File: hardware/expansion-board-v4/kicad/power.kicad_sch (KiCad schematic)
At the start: 39 parts, among them J9 MX1.25WT-2P BAT, U1 ME6211C33M5, U18 CH224K, U19 SY6970, U2 TPS7A2033PDBVR, U20 SY7069, U3 TPS7A2033PDBVR

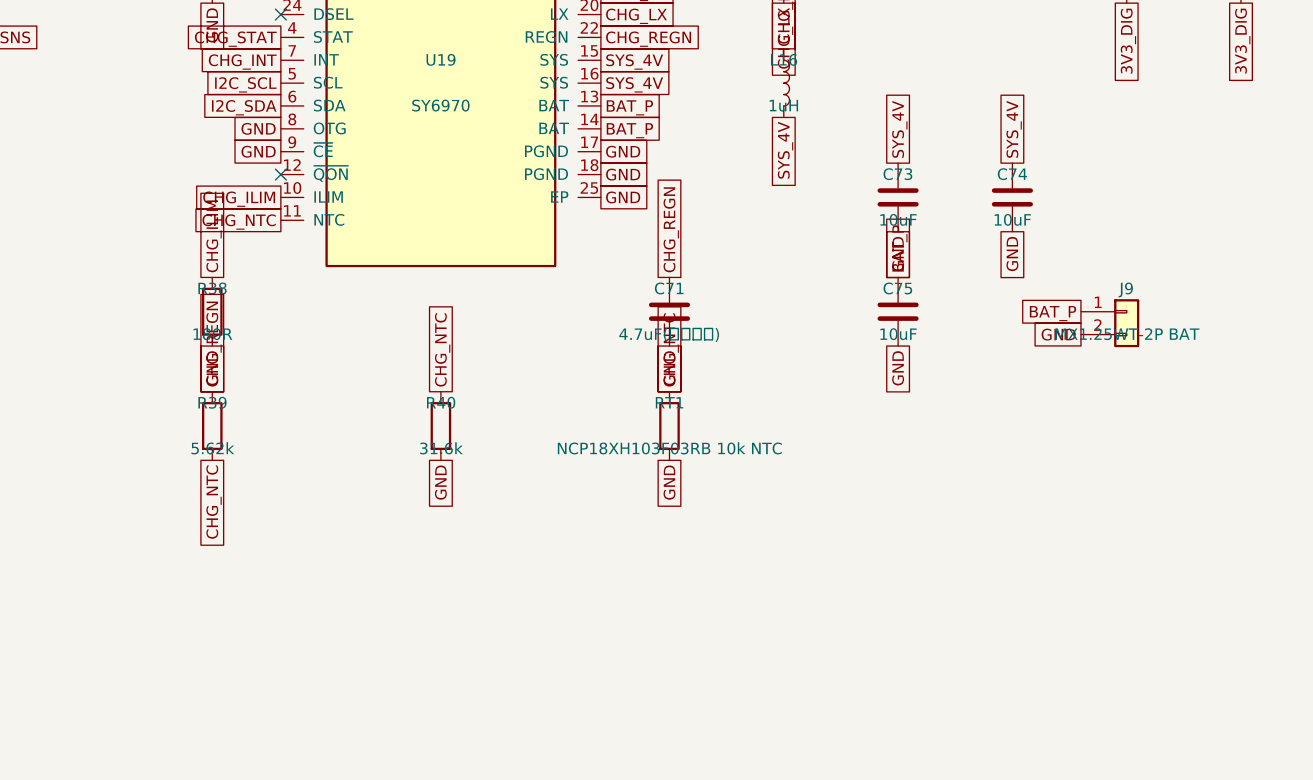
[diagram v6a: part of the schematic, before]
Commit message: v4.7: SW3 主电源键接 /QON + TCXO 输出隔直 + 覆铜填充参数固化
**SW3 主电源键**。电池在位时 SYS 恒供电，整板此前没有任何机械总电门：
微雪 Key3 只关得掉载板自己，而整机 5V 是扩展板升压产的；J1 的 40 脚里
没有一根电源控制线。唯一出路是 SY6970 的 BATFET——所以引 U19.12(/QON)
到板边的 TS24CA 侧按键（按住 1.25~2.25s 开机，BUS 拔掉时按 12~18s 硬复位），
不依赖固件。摆在 USB 口同侧贴板边 (97.882, 39.103)，R7/R8 那组往板内让 4mm 腾位。

封装按规格书 1:1：电气端子 1.2×0.6 中心距 3.4、固定脚 1.3×1.05 外缘跨度 5.3、
两个 φ0.55 定位孔在 X+0.70。两个坑记在封装 descr 里：①定位孔的 layers 必须写
「*.Cu」而不是「F&B.Cu」，否则 6 层板的内层覆铜照样压上来（每孔 5 条
hole_clearance、实际间距 0）；②孔心不能按「上下排焊盘空档的中心」推，那样
错 0.75mm、柱子插不进去。

**TCXO 输出隔直**。Epson brief sheet 的输出负载条件栏写死 DC cut = 0.01µF，
原设计 Y4.3 直连 BK4819 的 XI。补 C99(0402 100pF C0G) 串联 + R61(0402 10k)
负载，VHF_TCXO 拆成 VHF_TCXO_OUT / VHF_TCXO 两网。这里只能用 0402：两焊盘
净空 2.28mm，0603 含焊盘约 2.8mm 放不下，而 Y4 四周被 C76/C98/U21 夹死挪不开。
Y4 符号 pin1 由 EN 改 NC（选型库 fcfYN=N，无压控，悬空正确）。

**覆铜填充参数固化**（本次真正的回归修复）。ZONES.json 此前不含 fill 参数，
重放时 clearance 从板上的 0.15 退回 KiCad 默认 0.5，结果是 2 条网络断开、
4 个悬空端、4 个焊盘未连通——而 DRC 报 0 违例。「DRC 全绿」和「板子是错的」
可以同时成立，因为 zone 的 local clearance 不是 DRC 可见参数。现在导出/回填
clearance、min_thickness、pad_connection、thermal_gap/spoke、island_removal，
并加门禁：任何非 rule-area 的 zone 没拿到固化参数就炸。

装配助手加 v4.7-pwr / v4.7-nopwr，v4.6-* 转归档（元件数据不动，只在副标题
注明「无 SW3 电源键」）。SW3 属于电源区，不带电源版不贴它：207/82 → 180/67。

英文同步器补阶段 G（Airband）并加未登记阶段即炸的护栏：此前中文表加了 G，
而这里只认 A–F，stage 变量保持上一轮的 F 不变，19 个 airband 件被整段并进
「Stage F: External Interface」（1 件变 20 件），两边都不报错、产物看着完整。

Gerber/源包重出为 V4.7-20260913（制造内容与先前那版逐字节相同，仅时间戳行
不同；源包重出是为了让包内 PCB 与工作树一致）。

hardware 契约 80 条：76 通过、4 条 expansion-board-v3 的 RP_1V1 既存豁免不在
本次范围。interface.kicad_sch 工作树里有一份纯 uuid 变更、来源不明，未纳入。
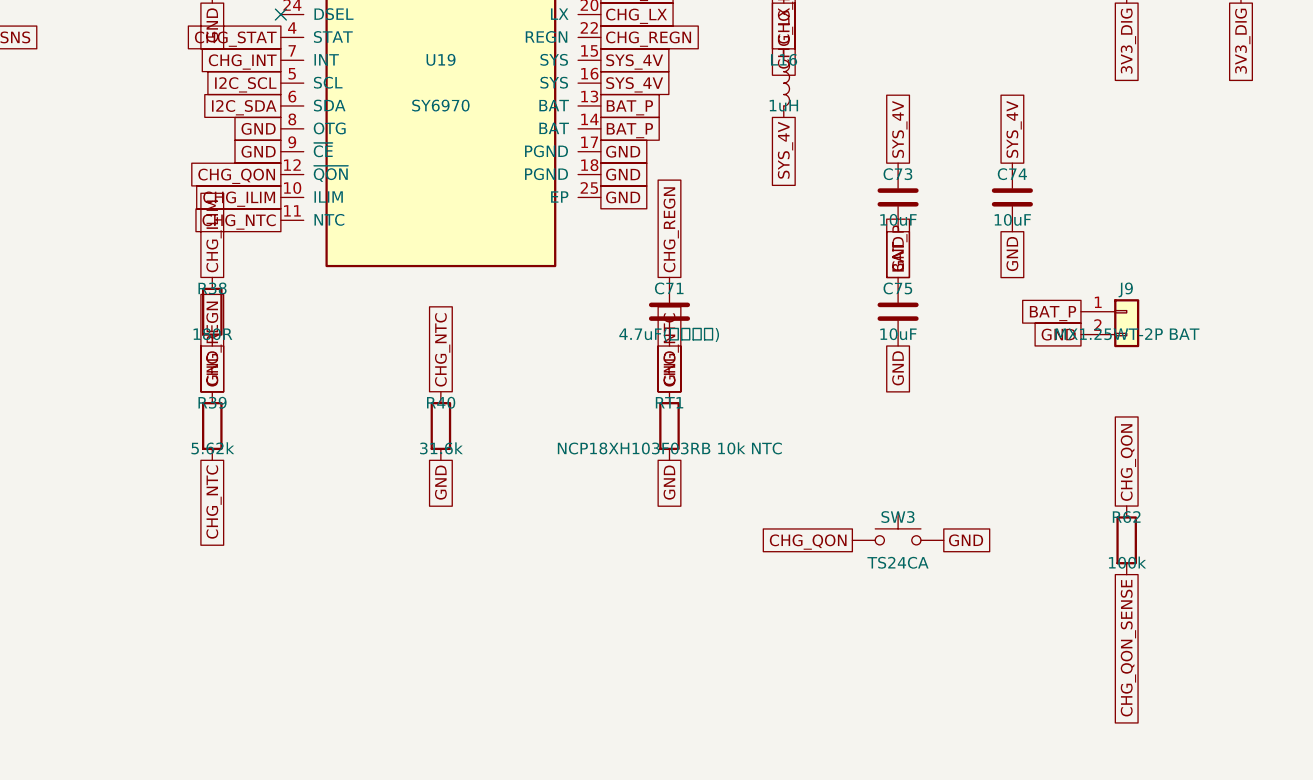
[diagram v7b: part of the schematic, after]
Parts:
- added R62: 100k, Resistor_SMD:R_0603_1608Metric, symbol Device:R
- added SW3: TS24CA, expansion-board-v4:SW_TS24CA_2x4_SideAct, symbol Switch:SW_Push
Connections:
- net GND: now also SW3.2
- net CHG_QON: now reaches U19.12 (~{QON})
- net CHG_QON: now also R62.1, SW3.1
- new net CHG_QON_SENSE: R62.2
- no-connect marks 10 -> 9
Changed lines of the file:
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@@
 		(effects (font (size 1.27 1.27)) (justify right))
 	)
-	(no_connect
-		(at 134.62 175.26)
+	(global_label "CHG_QON"
+		(shape passive)
+		(at 134.62 175.26 180)
+		(effects (font (size 1.27 1.27)) (justify right))
 	)
 	(global_label "CHG_ILIM"
@@
 		(effects (font (size 1.27 1.27)) (justify right))
 	)
+	(symbol
+		(lib_id "Switch:SW_Push")
+		(at 203.2 215.9 0)
+		(unit 1)
+		(exclude_from_sim no)
+		(in_bom yes)
+		(on_board yes)
+		(dnp no)
+		(property "Reference" "SW3"
+			(at 203.2 213.36 0)
+			(effects (font (size 1.27 1.27)))
+		)
+		(property "Value" "TS24CA"
+			(at 203.2 218.44 0)
+			(effects (font (size 1.27 1.27)))
+		)
+		(property "Footprint" "expansion-board-v4:SW_TS24CA_2x4_SideAct"
+			(at 203.2 220.98 0)
+			(effects (font (size 1.27 1.27))
+				(hide yes))
+		)
+		(property "Datasheet" "~"
+			(at 203.2 223.52 0)
+			(effects (font (size 1.27 1.27))
+				(hide yes))
+		)
+		(pin "1"
+		)
+		(pin "2"
+		)
+		(instances
+			(project "expansion-board-v4"
+				(path "/10000000-0000-4000-8000-000000000001/20000000-0000-4000-8000-000000000001"
+					(reference "SW3")
+					(unit 1)
+				)
+			)
+		)
+	)
+	(global_label "CHG_QON"
+		(shape passive)
+		(at 198.12 215.9 180)
+		(effects (font (size 1.27 1.27)) (justify right))
+	)
+	(global_label "GND"
+		(shape passive)
+		(at 208.28 215.9 0)
+		(effects (font (size 1.27 1.27)) (justify left))
+	)
+	(symbol
+		(lib_id "Device:R")
+		(at 228.6 215.9 0)
+		(unit 1)
+		(exclude_from_sim no)
+		(in_bom yes)
+		(on_board yes)
+		(dnp no)
+		(property "Reference" "R62"
+			(at 228.6 213.36 0)
+			(effects (font (size 1.27 1.27)))
+		)
+		(property "Value" "100k"
+			(at 228.6 218.44 0)
+			(effects (font (size 1.27 1.27)))
+		)
+		(property "Footprint" "Resistor_SMD:R_0603_1608Metric"
+			(at 228.6 220.98 0)
+			(effects (font (size 1.27 1.27))
+				(hide yes))
+		)
+		(property "Datasheet" "~"
+			(at 228.6 223.52 0)
+			(effects (font (size 1.27 1.27))
+				(hide yes))
+		)
+		(pin "1"
+		)
+		(pin "2"
+		)
+		(instances
+			(project "expansion-board-v4"
+				(path "/10000000-0000-4000-8000-000000000001/20000000-0000-4000-8000-000000000001"
+					(reference "R62")
+					(unit 1)
+				)
+			)
+		)
+	)
+	(global_label "CHG_QON"
+		(shape passive)
+		(at 228.6 212.09 270)
+		(effects (font (size 1.27 1.27)) (justify left))
+	)
+	(global_label "CHG_QON_SENSE"
+		(shape passive)
+		(at 228.6 219.71 90)
+		(effects (font (size 1.27 1.27)) (justify right))
+	)

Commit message: v4.7: 撤掉误并入原理图的 R62/CHG_QON_SENSE
1ef0dd5 提交 power.kicad_sch 时，把另一路 session 正在做的 R62（/QON 经 100k
引到 J1.8 的按键感知电阻）一起卷了进来。那条线的评审结论是不采纳，判据见
release/README.md；PCB 从头到尾没有 R62，所以板子一直是对的，错的是原理图。

后果是原理图与 PCB 不一致，而现有门禁看不见：
test_every_pad_net_matches_the_schematic 遍历的是 PCB 上的焊盘，"原理图有而
PCB 没有的元件"落在它的盲区；test_v4_release_package_is_revisioned_and_matches_source
只逐字节比对包内 PCB，不比对原理图。两条都绿，板子却是矛盾的。

恢复来源是 release 里的 KiCad 源包——它在 02:37 打包，早于污染写入，
包内 kicad/power.kicad_sch 的 md5 1e8ad671 正是干净版（R62=0、SW3=2），
比工作树可信。恢复后与源包逐字节相同，源包/源文件/PCB 三者重新自洽。

同时把重放链的输入清干净（在 internal/，不进本仓）：PLACEMENT.py 和
ROUTES.json 此前整份是从对方那块含 R62 的板导出的——ROUTES.json 有 1873 段
走线而当前板只有 1784 段，正好差报告里写的"新增 89 段"。没有手工删条目，
而是用 export_routes.py / export_placement.py 从当前干净 PCB 重新导出。
gen_jlc_smt.py 的 VARIANT_PWR 去掉 R62（顺手删掉重复的 | {"SW3"}）。
对方为 R62 写的 check_qon_assembly_v47.py 断言"R62 必须存在"，方案撤销后必然
失败且会误导，移到 internal/qon-parity-repair/ 归档，它不在重放链上。

验证：隔离副本跑完整 rebuild.sh，重放板与工作区板 229 位号、1784 段走线、
487 过孔逐项一致，位号差异为空，R62 与 CHG_QON_SENSE 均为 0，而 SW3 的
CHG_QON 网络 10 处完整保留；真缺线/孤立铜/焊盘未连通均 0，铜层与丝印 DRC
均 0，文档坐标 414 处 0 不符。hardware 契约 80 条仅剩 4 条 v3 既存豁免。
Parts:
- removed R62: 100k, Resistor_SMD:R_0603_1608Metric, symbol Device:R
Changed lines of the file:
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@@
-	)
-	(symbol
-		(lib_id "Device:R")
-		(at 228.6 215.9 0)
-		(unit 1)
-		(exclude_from_sim no)
-		(in_bom yes)
-		(on_board yes)
-		(dnp no)
-		(property "Reference" "R62"
-			(at 228.6 213.36 0)
-			(effects (font (size 1.27 1.27)))
-		)
-		(property "Value" "100k"
-			(at 228.6 218.44 0)
-			(effects (font (size 1.27 1.27)))
-		)
-		(property "Footprint" "Resistor_SMD:R_0603_1608Metric"
-			(at 228.6 220.98 0)
-			(effects (font (size 1.27 1.27))
-				(hide yes))
-		)
-		(property "Datasheet" "~"
-			(at 228.6 223.52 0)
-			(effects (font (size 1.27 1.27))
-				(hide yes))
-		)
-		(pin "1"
-		)
-		(pin "2"
-		)
-		(instances
-			(project "expansion-board-v4"
-				(path "/10000000-0000-4000-8000-000000000001/20000000-0000-4000-8000-000000000001"
-					(reference "R62")
-					(unit 1)
-				)
-			)
-		)
-	)
-	(global_label "CHG_QON"
-		(shape passive)
-		(at 228.6 212.09 270)
-		(effects (font (size 1.27 1.27)) (justify left))
-	)
-	(global_label "CHG_QON_SENSE"
-		(shape passive)
-		(at 228.6 219.71 90)
-		(effects (font (size 1.27 1.27)) (justify right))
 	)
 	(symbol
